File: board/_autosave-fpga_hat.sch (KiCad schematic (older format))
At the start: 86 parts, among them J1 2x20, J2 AudioJack3, J3 Conn_02x06_Top_Bottom, J4 Conn_02x06_Top_Bottom, J5 Conn_02x06_Top_Bottom, J6 Conn_01x02, SW1 PTS815, SW2 PTS815, SW3 PTS815, SW4 PTS815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

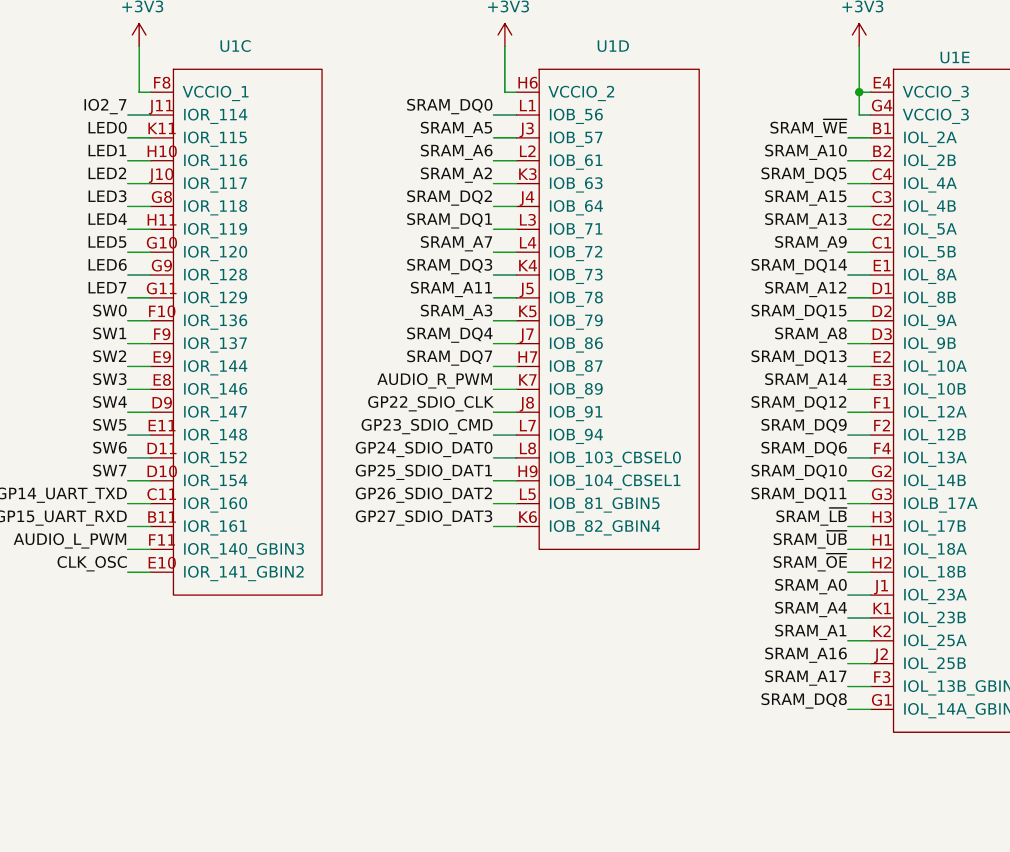
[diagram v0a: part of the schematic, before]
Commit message: SRAM escaped. Some work on FPGA power routing. Some SRAM pinswapping.
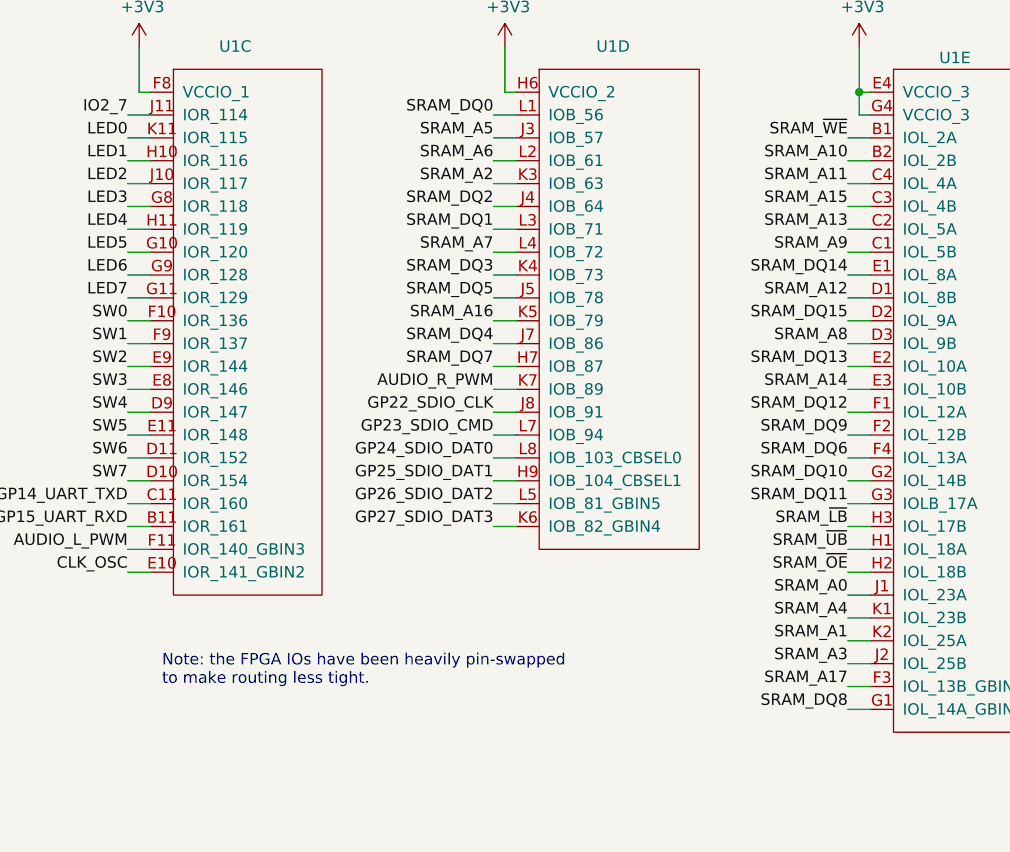
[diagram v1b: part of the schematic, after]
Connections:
- net SRAM_A11: now also U1.C4 (IOL_4A); no longer U1.J5 (IOB_78)
- net SRAM_A16: now also U1.K5 (IOB_79); no longer U1.J2 (IOL_25B)
- net SRAM_A3: now also U1.J2 (IOL_25B); no longer U1.K5 (IOB_79)
- net SRAM_DQ5: now also U1.J5 (IOB_78); no longer U1.C4 (IOL_4A)
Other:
- note added: "Note: the FPGA IOs have been heavily pin-swapped\nto make routing less tight."
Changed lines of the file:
@@
 Text Label 5850 2500 2    50   ~ 0
 SRAM_DQ4
-Text Label 7400 1800 2    50   ~ 0
+Text Label 5850 2300 2    50   ~ 0
 SRAM_DQ5
 Text Label 7400 3000 2    50   ~ 0
@@
 Text Label 7400 1700 2    50   ~ 0
 SRAM_A10
-Text Label 5850 2300 2    50   ~ 0
+Text Label 7400 1800 2    50   ~ 0
 SRAM_A11
 Text Label 7400 2300 2    50   ~ 0
@@
 Text Label 5850 1600 2    50   ~ 0
 SRAM_A5
-Text Label 5850 2400 2    50   ~ 0
+Text Label 7400 3900 2    50   ~ 0
 SRAM_A3
 Text Label 7400 3500 2    50   ~ 0
 SRAM_~OE
-Text Label 7400 3900 2    50   ~ 0
+Text Label 5850 2400 2    50   ~ 0
 SRAM_A16
 Text Label 7400 2600 2    50   ~ 0
@@
 Text Label 7400 2500 2    50   ~ 0
 SRAM_A8
+Text Notes 4400 4000 0    50   ~ 0
+Note: the FPGA IOs have been heavily pin-swapped\nto make routing less tight.
 $EndSCHEMATC
